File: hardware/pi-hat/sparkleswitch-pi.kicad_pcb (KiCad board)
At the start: 2 copper layers, 65 x 56 mm, 25 parts, among them J1 Conn_01x02, J2 Conn_02x06_Odd_Even, P1 CONN_02X20, U1 74HCT245, U2 74HCT245, U3 74HCT245, U4 PC817, U5 PC817, U6 PC817, U7 PC817

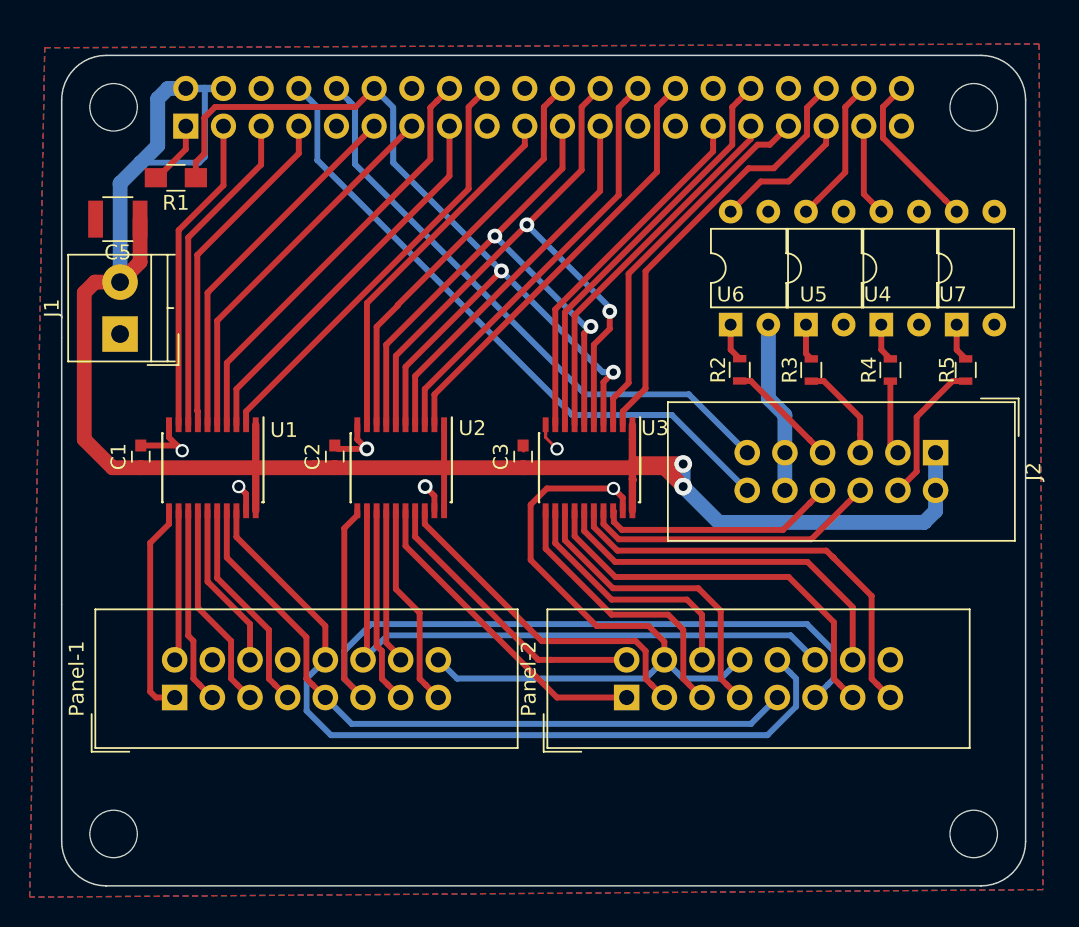
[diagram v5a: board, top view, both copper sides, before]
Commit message: Add helpful silkscreen markings.
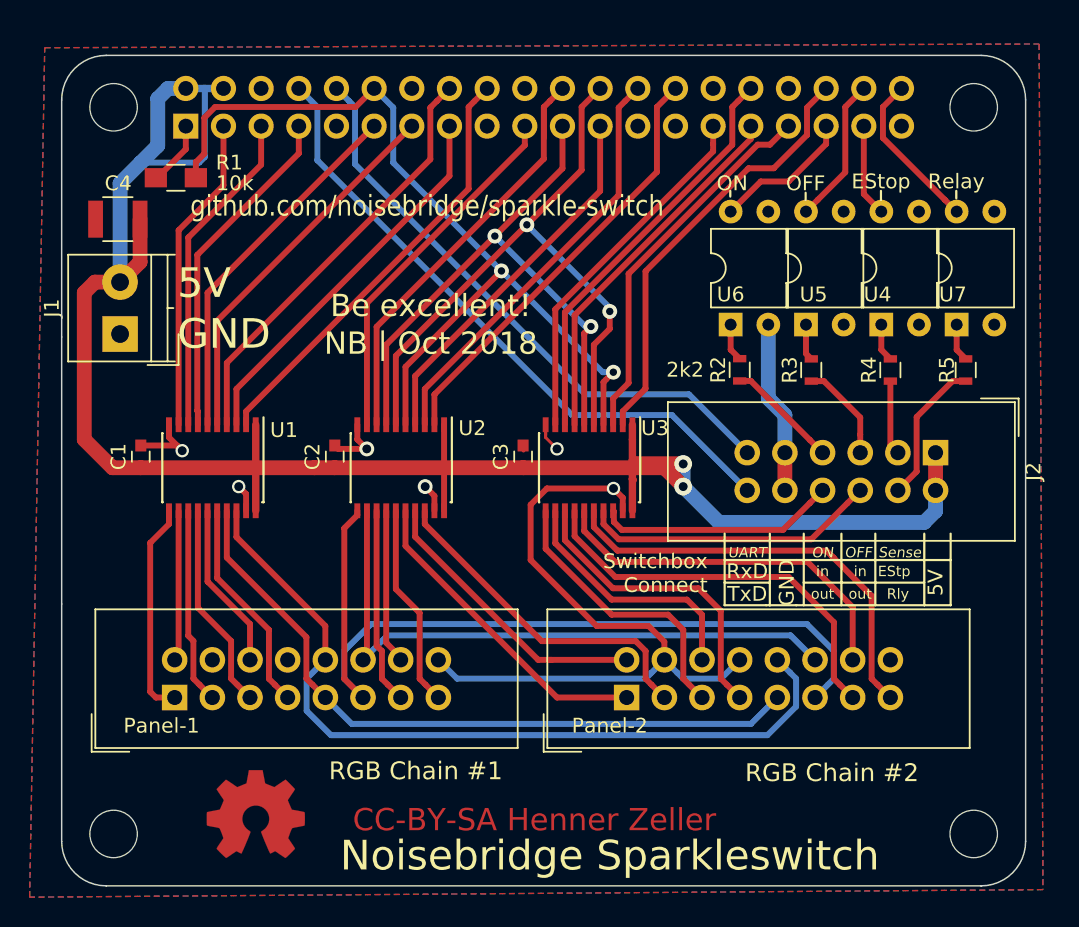
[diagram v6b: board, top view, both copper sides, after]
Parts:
- added REF***: OSHW-Symbol_6.7x6mm_Copper, Symbols:OSHW-Symbol_6.7x6mm_Copper, F.Cu at (213.1, 145.2)
- R2, R3, R4, R5: value R -> 2k2
- renumbered C5 to C4
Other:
- board text added: "5V"
- board text added: "Be excellent!"
- board text added: "CC-BY-SA Henner Zeller"
- board text added: "EStop"
- board text added: "EStp"
- board text added: "GND"
- board text added: "NB | Oct 2018"
- board text added: "Noisebridge Sparkleswitch"
- board text added: "OFF"
- board text added: "ON"
- board text added: "RGB Chain #1"
- board text added: "RGB Chain #2"
- board text added: "Relay"
- board text added: "Rly"
- board text added: "RxD"
- board text added: "Sense"
- board text added: "Switchbox Connect"
- board text added: "TxD"
- board text added: "UART"
- board text added: "github.com/noisebridge/sparkle-switch"
- board text added: "in"
- board text added: "out"
